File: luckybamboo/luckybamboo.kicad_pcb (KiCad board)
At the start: 4 copper layers, 70.7 x 53.3 mm, 148 parts, among them J1 NEIGHBOR1, J10 TEST_2P, J11 TEST_2P, J12 TEST_2P, J13 TEST_2P, J14 TEST_2P, J15 TEST_2P, J16 TEST_2P, J17 Conn_Coaxial, J18 Conn_Coaxial, J19 TEST_2P, J2 NEIGHBOR2, J20 TEST_2P, J21 TEST_2P, J22 TEST_2P, J23 TEST_2P, J24 TEST_2P, J25 TEST_2P, J26 TEST_2P, J27 TEST_2P, J28 TEST_2P, J29 TEST_2P, J3 Conn_01x08, J30 TEST_2P, J31 TEST_2P, J32 TEST_2P, J33 TEST_2P, J4 Conn_01x08, J5 Conn_01x08, J6 Conn_01x08, J7 BONUS_ROW, J8 TEST_2P, J9 TEST_2P, U1 ADF7242, U10 ADF7242_balun, U11 ADF7242_balun, U12 BGA7H1N6, U13 BGA7H1N6, U14 ADF7242_balun, U15 ADF7242_balun, U16 ADF7242_balun, U17 ADF7242_balun, U2 ADF7242, U3 ADF7242, U4 ADF7242, U5 SKY13322, U6 BGA7H1N6, U7 BGA7H1N6, U8 ADF7242_balun, U9 ADF7242_balun, X1 XTAL4PIN, X2 XTAL4PIN, X3 XTAL4PIN, X4 XTAL4PIN

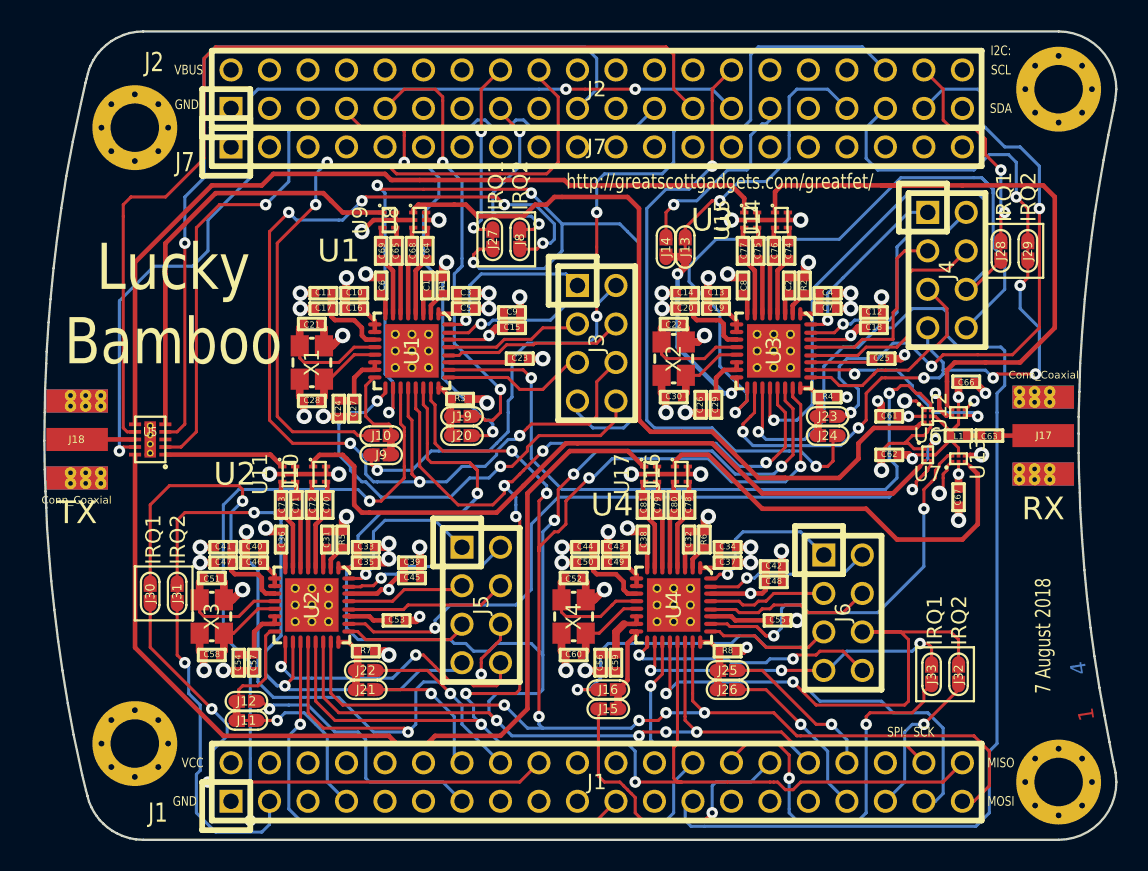
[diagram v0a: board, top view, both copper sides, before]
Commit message: Completed new amplifier/splitter section in schematic and layout.
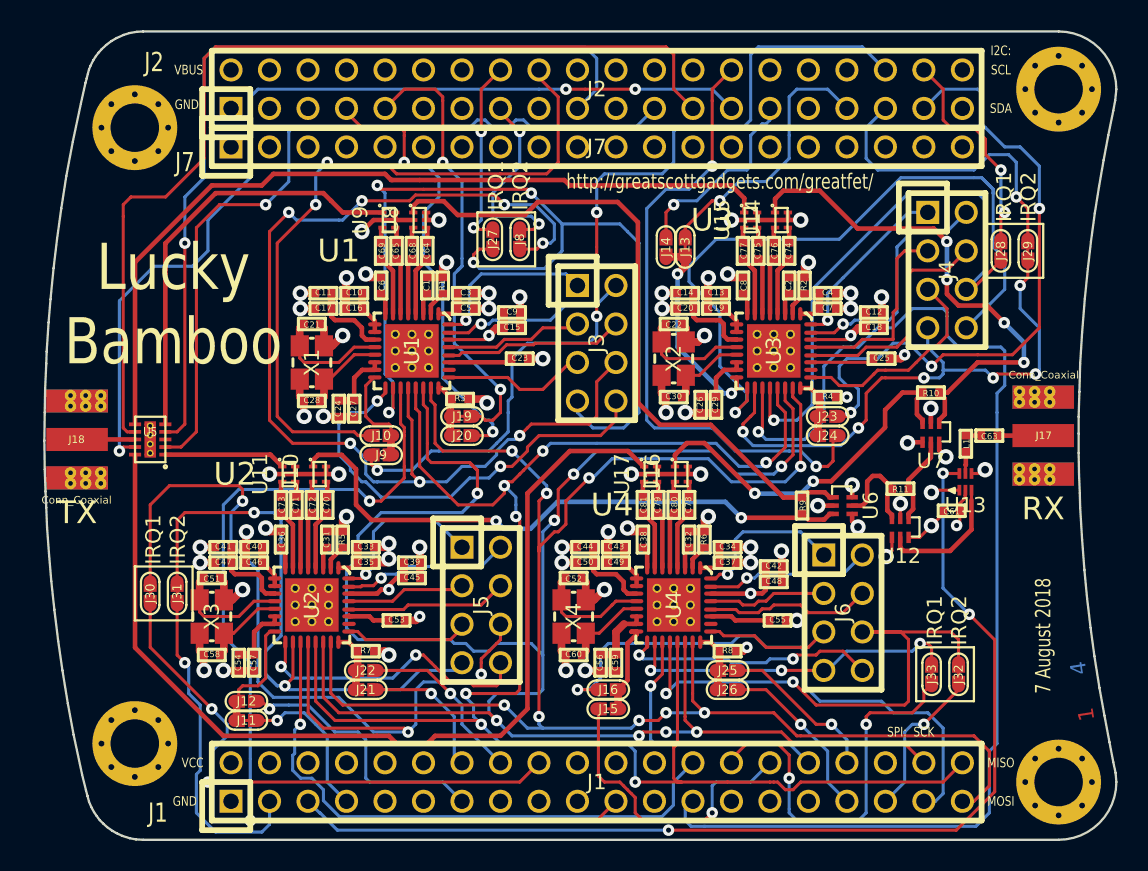
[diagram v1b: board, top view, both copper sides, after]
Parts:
- removed C62, C66, C67: 1nF, gsg-modules:0402
- added R10: 100, gsg-modules:0402, F.Cu at (168.1, 92.4)
- added R11: 100, gsg-modules:0402, F.Cu at (166.1, 98.8)
- added R9: 100, gsg-modules:0402, F.Cu at (159.6, 99.9)
- U12, U6, U7: value BGA7H1N6 -> HHM2293A1; footprint gsg-modules:TSNP-6-2 -> gsg-modules:HHM2293A1
- U13: footprint gsg-modules:TSNP-6-2 -> gsg-modules:BGA7H1N6
- moved U12 10.7 mm to (166.1, 103.7), turned to 180 degrees
- moved C61 7.47 mm to (169.5, 100.2), turned to 0 degrees
- moved U6 6.73 mm to (164.6, 99.9), turned to 270 degrees
- moved U13 1.59 mm to (170.4, 98.3), turned to 180 degrees
- moved U7 0.92 mm to (168.1, 97.4)
- moved L1 0.72 mm to (170.4, 95.8), turned to 90 degrees
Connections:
- C61 pad 1: VCC -> GND
- C61 pad 2: GND -> VCC
- C68 pad 1: /RFIN1_N -> Net-(C68-Pad1)
- C68 pad 2: Net-(C68-Pad2) -> /RFIN1_N
- C69 pad 1: /RFOUT1_N -> Net-(C69-Pad1)
- C69 pad 2: Net-(C69-Pad2) -> /RFOUT1_N
- C72 pad 1: /RFIN2_N -> Net-(C72-Pad1)
- C72 pad 2: Net-(C72-Pad2) -> /RFIN2_N
- C73 pad 1: /RFOUT2_N -> Net-(C73-Pad1)
- C73 pad 2: Net-(C73-Pad2) -> /RFOUT2_N
- C76 pad 1: /RFIN3_N -> Net-(C76-Pad1)
- C76 pad 2: Net-(C76-Pad2) -> /RFIN3_N
- C77 pad 1: /RFOUT3_N -> Net-(C77-Pad1)
- C77 pad 2: Net-(C77-Pad2) -> /RFOUT3_N
- C80 pad 1: /RFIN4_N -> Net-(C80-Pad1)
- C80 pad 2: Net-(C80-Pad2) -> /RFIN4_N
- C81 pad 1: /RFOUT4_N -> Net-(C81-Pad1)
- C81 pad 2: Net-(C81-Pad2) -> /RFOUT4_N
- U10 pad 3: Net-(C72-Pad2) -> Net-(C72-Pad1)
- U11 pad 3: Net-(C73-Pad2) -> Net-(C73-Pad1)
- U12 pad 1: GND -> Net-(R11-Pad2)
- U12 pad 2: VCC -> GND
- U12 pad 3: /RFIN3 -> Net-(R11-Pad1)
- U12 pad 5: /RFIN -> Net-(U12-Pad5)
- U12 pad 6: /RXEN3 -> GND
- U13 pad 3: /RFIN4 -> Net-(U12-Pad5)
- U13 pad 6: /RXEN4 -> /P4_10
- U14 pad 3: Net-(C76-Pad2) -> Net-(C76-Pad1)
- U15 pad 3: Net-(C77-Pad2) -> Net-(C77-Pad1)
- U16 pad 3: Net-(C80-Pad2) -> Net-(C80-Pad1)
- U17 pad 3: Net-(C81-Pad2) -> Net-(C81-Pad1)
- U6 pad 1: GND -> /RFIN1
- U6 pad 2: VCC -> GND
- U6 pad 3: /RFIN1 -> /RFIN2
- U6 pad 5: /RFIN -> Net-(R11-Pad1)
- U6 pad 6: /RXEN1 -> GND
- U7 pad 1: GND -> /RFIN3
- U7 pad 2: VCC -> GND
- U7 pad 3: /RFIN2 -> /RFIN4
- U7 pad 5: /RFIN -> Net-(R11-Pad2)
- U7 pad 6: /RXEN2 -> GND
- U8 pad 3: Net-(C68-Pad2) -> Net-(C68-Pad1)
- U9 pad 3: Net-(C69-Pad2) -> Net-(C69-Pad1)
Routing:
- net /P4_10: track 0.00 -> 70.7 mm, vias 0 -> 3
- net /RXEN2: track 48.2 -> 0.00 mm, vias 2 -> 0
- net /RXEN1: track 45.9 -> 0.00 mm, vias 2 -> 0
- net /RFIN1: track 82.0 -> 44.3 mm
- net /RFIN4: track 54.7 -> 24.6 mm, vias 0 -> 2
- net /RXEN4: track 28.9 -> 0.00 mm, vias 2 -> 0
- net /RFIN2: track 64.5 -> 39.9 mm, vias 0 -> 2
- net /RFIN3: track 58.0 -> 33.8 mm, vias 0 -> 4
- net /RXEN3: track 13.6 -> 0.00 mm, vias 2 -> 0
- net GND: track 128.3 -> 118.5 mm, vias 66 -> 67
- net Net-(U12-Pad5): track 0.00 -> 8.65 mm
- net /RFIN: track 8.58 -> 1.59 mm
- net Net-(R11-Pad1): track 0.00 -> 6.81 mm
- net Net-(R11-Pad2): track 0.00 -> 5.89 mm
- net VCC: track 32.2 -> 27.0 mm, vias 12 -> 9
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
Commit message: Fixed clearances and silk screen date
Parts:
- turned C68 to 270 degrees
- turned C69 to 270 degrees
- turned C72 to 270 degrees
- turned C73 to 270 degrees
- turned C76 to 270 degrees
- turned C77 to 270 degrees
- turned C80 to 270 degrees
- turned C81 to 270 degrees
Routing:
- net Net-(C53-Pad2): track 4.50 -> 3.05 mm
- net Net-(C77-Pad2): track 1.03 -> 0.00 mm
- net Net-(C77-Pad1): track 0.00 -> 1.03 mm
- net Net-(C76-Pad2): track 1.03 -> 0.00 mm
- net Net-(C76-Pad1): track 0.00 -> 1.03 mm
- net Net-(C69-Pad2): track 1.03 -> 0.00 mm
- net Net-(C69-Pad1): track 0.00 -> 1.03 mm
- net Net-(C68-Pad2): track 1.03 -> 0.00 mm
- net Net-(C68-Pad1): track 0.00 -> 1.03 mm
- net Net-(C73-Pad2): track 1.03 -> 0.00 mm
- net Net-(C73-Pad1): track 0.00 -> 1.03 mm
- net Net-(C81-Pad2): track 1.03 -> 0.00 mm
- net Net-(C81-Pad1): track 0.00 -> 1.03 mm
- net Net-(C80-Pad2): track 1.03 -> 0.00 mm
- net Net-(C80-Pad1): track 0.00 -> 1.03 mm
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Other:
- net class Default: clearance 0.1524 -> 0.127
- rule trace_clearance: 0.1524 -> 0.127
- rule trace_min: 0.2032 -> 0.127
- board text added: "3 January 2019"
- board text removed: "7 August 2018"

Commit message: JASMINE: Revised charge rate config; Added DNP JST connector; Added DNP screw terminal; Added load switch w/ LED indicator; Updated labeling on silkscreen LUCKY BAMBOO: updated soldermask clearance
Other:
- rule pad_to_mask_clearance: 0.127 -> 0.0762
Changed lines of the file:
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@@
     (pad_size 0.25 0.7)
     (pad_drill 0)
-    (pad_to_mask_clearance 0.127)
-    (solder_mask_min_width 0.25)
+    (pad_to_mask_clearance 0.0762)
     (pad_to_paste_clearance_ratio -0.05)
     (aux_axis_origin 0 0)
@@
   (segment (start 134.10692 87.2109) (end 134.10692 84.35848) (width 0.3048) (layer F.Cu) (net 176))
   (segment (start 134.10692 84.35848) (end 134.874 83.5914) (width 0.3048) (layer F.Cu) (net 176))
-  (segment (start 133.858 82.5246) (end 133.858 81.609) (width 0.3048) (layer F.Cu) (net 217))
-  (segment (start 133.858 81.609) (end 133.941 81.526) (width 0.3048) (layer F.Cu) (net 217))
   (segment (start 133.60908 87.2109) (end 133.60908 83.84032) (width 0.3048) (layer F.Cu) (net 177))
   (segment (start 133.60908 83.84032) (end 133.858 83.5914) (width 0.3048) (layer F.Cu) (net 177))
-  (segment (start 131.826 82.5246) (end 131.826 81.609) (width 0.3048) (layer F.Cu) (net 218))
-  (segment (start 131.826 81.609) (end 131.909 81.526) (width 0.3048) (layer F.Cu) (net 218))
   (segment (start 127.50292 103.9749) (end 127.50292 101.12248) (width 0.3048) (layer F.Cu) (net 178))
   (segment (start 127.50292 101.12248) (end 128.27 100.3554) (width 0.3048) (layer F.Cu) (net 178))
@@
   (segment (start 126.238 99.2886) (end 126.238 98.373) (width 0.3048) (layer F.Cu) (net 180))
   (segment (start 126.238 98.373) (end 126.155 98.29) (width 0.3048) (layer F.Cu) (net 180))
-  (segment (start 127.254 99.2886) (end 127.254 98.373) (width 0.3048) (layer F.Cu) (net 219))
-  (segment (start 127.254 98.373) (end 127.337 98.29) (width 0.3048) (layer F.Cu) (net 219))
   (segment (start 127.00508 103.9749) (end 127.00508 100.60432) (width 0.3048) (layer F.Cu) (net 181))
   (segment (start 127.00508 100.60432) (end 127.254 100.3554) (width 0.3048) (layer F.Cu) (net 181))
-  (segment (start 125.222 99.2886) (end 125.222 98.373) (width 0.3048) (layer F.Cu) (net 220))
-  (segment (start 125.222 98.373) (end 125.305 98.29) (width 0.3048) (layer F.Cu) (net 220))
   (segment (start 157.98292 87.2109) (end 157.98292 84.35848) (width 0.3048) (layer F.Cu) (net 182))
   (segment (start 157.98292 84.35848) (end 158.75 83.5914) (width 0.3048) (layer F.Cu) (net 182))
-  (segment (start 157.734 82.5246) (end 157.734 81.609) (width 0.3048) (layer F.Cu) (net 221))
-  (segment (start 157.734 81.609) (end 157.817 81.526) (width 0.3048) (layer F.Cu) (net 221))
   (segment (start 157.48508 87.2109) (end 157.48508 83.84032) (width 0.3048) (layer F.Cu) (net 183))
   (segment (start 157.48508 83.84032) (end 157.734 83.5914) (width 0.3048) (layer F.Cu) (net 183))
-  (segment (start 155.702 82.5246) (end 155.702 81.609) (width 0.3048) (layer F.Cu) (net 222))
-  (segment (start 155.702 81.609) (end 155.785 81.526) (width 0.3048) (layer F.Cu) (net 222))
   (segment (start 151.37892 103.9749) (end 151.37892 101.12248) (width 0.3048) (layer F.Cu) (net 184))
   (segment (start 151.37892 101.12248) (end 152.146 100.3554) (width 0.3048) (layer F.Cu) (net 184))
@@
   (segment (start 150.114 99.2886) (end 150.114 98.373) (width 0.3048) (layer F.Cu) (net 186))
   (segment (start 150.114 98.373) (end 150.031 98.29) (width 0.3048) (layer F.Cu) (net 186))
-  (segment (start 151.13 99.2886) (end 151.13 98.373) (width 0.3048) (layer F.Cu) (net 223))
-  (segment (start 151.13 98.373) (end 151.213 98.29) (width 0.3048) (layer F.Cu) (net 223))
   (segment (start 150.88108 103.9749) (end 150.88108 100.60432) (width 0.3048) (layer F.Cu) (net 187))
   (segment (start 150.88108 100.60432) (end 151.13 100.3554) (width 0.3048) (layer F.Cu) (net 187))
-  (segment (start 149.098 99.2886) (end 149.098 98.373) (width 0.3048) (layer F.Cu) (net 224))
-  (segment (start 149.098 98.373) (end 149.181 98.29) (width 0.3048) (layer F.Cu) (net 224))
   (segment (start 136.3091 87.91194) (end 137.13206 87.91194) (width 0.2032) (layer F.Cu) (net 188))
   (segment (start 138.43 84.582) (end 144.018 84.582) (width 0.2032) (layer B.Cu) (net 188))
@@
   (segment (start 161.53 98.26) (end 160.34 98.26) (width 0.3048) (layer F.Cu) (net 216))
   (segment (start 165.08 94.71) (end 161.53 98.26) (width 0.3048) (layer F.Cu) (net 216))
+  (segment (start 133.858 82.5246) (end 133.858 81.609) (width 0.3048) (layer F.Cu) (net 217))
+  (segment (start 133.858 81.609) (end 133.941 81.526) (width 0.3048) (layer F.Cu) (net 217))
+  (segment (start 131.826 82.5246) (end 131.826 81.609) (width 0.3048) (layer F.Cu) (net 218))
+  (segment (start 131.826 81.609) (end 131.909 81.526) (width 0.3048) (layer F.Cu) (net 218))
+  (segment (start 127.254 99.2886) (end 127.254 98.373) (width 0.3048) (layer F.Cu) (net 219))
+  (segment (start 127.254 98.373) (end 127.337 98.29) (width 0.3048) (layer F.Cu) (net 219))
+  (segment (start 125.222 99.2886) (end 125.222 98.373) (width 0.3048) (layer F.Cu) (net 220))
+  (segment (start 125.222 98.373) (end 125.305 98.29) (width 0.3048) (layer F.Cu) (net 220))
+  (segment (start 157.734 82.5246) (end 157.734 81.609) (width 0.3048) (layer F.Cu) (net 221))
+  (segment (start 157.734 81.609) (end 157.817 81.526) (width 0.3048) (layer F.Cu) (net 221))
+  (segment (start 155.702 82.5246) (end 155.702 81.609) (width 0.3048) (layer F.Cu) (net 222))
+  (segment (start 155.702 81.609) (end 155.785 81.526) (width 0.3048) (layer F.Cu) (net 222))
+  (segment (start 151.13 99.2886) (end 151.13 98.373) (width 0.3048) (layer F.Cu) (net 223))
+  (segment (start 151.13 98.373) (end 151.213 98.29) (width 0.3048) (layer F.Cu) (net 223))
+  (segment (start 149.098 99.2886) (end 149.098 98.373) (width 0.3048) (layer F.Cu) (net 224))
+  (segment (start 149.098 98.373) (end 149.181 98.29) (width 0.3048) (layer F.Cu) (net 224))
   (segment (start 166.6268 98.7754) (end 166.6268 98.75) (width 0.3048) (layer F.Cu) (net 225))
   (segment (start 166.93 99.0786) (end 166.6268 98.7754) (width 0.3048) (layer F.Cu) (net 225))

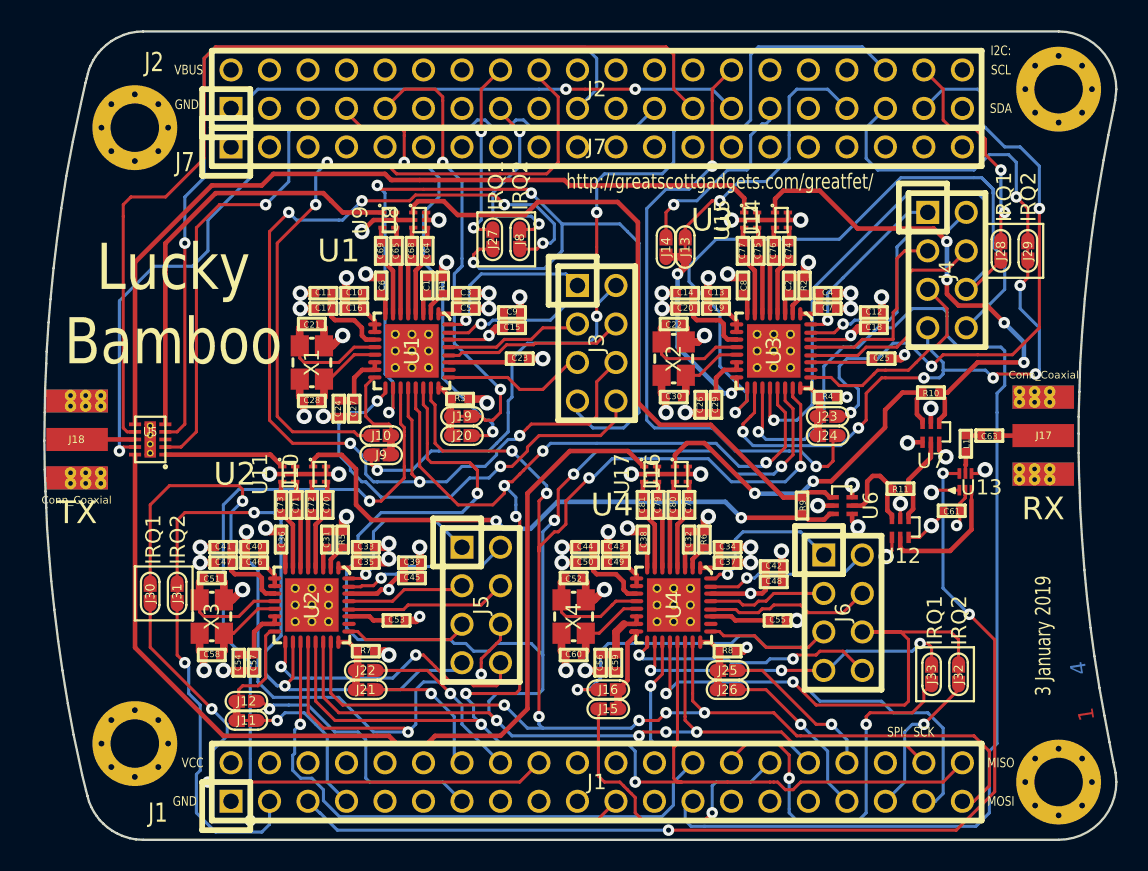
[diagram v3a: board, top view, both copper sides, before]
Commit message: BOM: Changed SMA connectors to RP-SMA and changed SPORT header
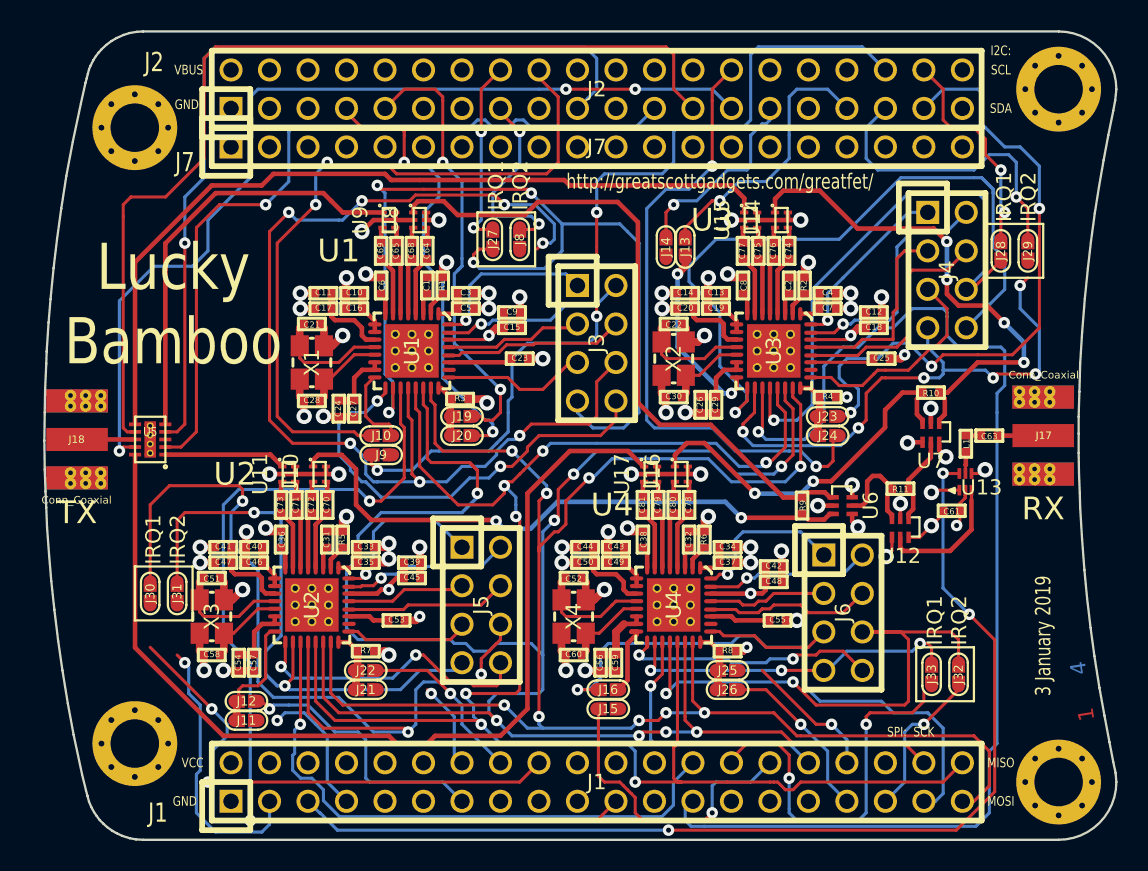
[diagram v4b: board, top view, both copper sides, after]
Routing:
- net /P5_2: track 9.19 -> 5.77 mm
- net /P4_9: track 21.7 -> 18.2 mm
- net /P1_8: track 36.8 -> 33.9 mm
- net /P9_6: track 11.4 -> 9.51 mm
- net /DR3: track 24.1 -> 22.2 mm
- net /P1_0: track 10.9 -> 9.50 mm
- net /~CS~4: track 5.40 -> 4.11 mm
- net /~CS~2: track 5.40 -> 4.11 mm
- net /~CS~3: track 5.49 -> 4.19 mm
- net /~CS~1: track 7.41 -> 6.11 mm
- net /P6_3: track 60.6 -> 59.3 mm
- net /P2_6: track 14.2 -> 12.9 mm
- net /P2_1: track 21.5 -> 20.2 mm
- net /DR2: track 8.99 -> 7.69 mm
- net /DR4: track 5.97 -> 4.70 mm
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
